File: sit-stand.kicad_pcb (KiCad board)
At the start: 2 copper layers, 158.8 x 50.8 mm, 69 parts, among them J1 USB_OTG, J2 CONN_02X03, J3 CONN_01X04, J4 CONN_01X16, J5 CONN_01X06, J6 CONN_02X04, U1 APA102, U10 APA102, U11 APA102, U12 APA102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

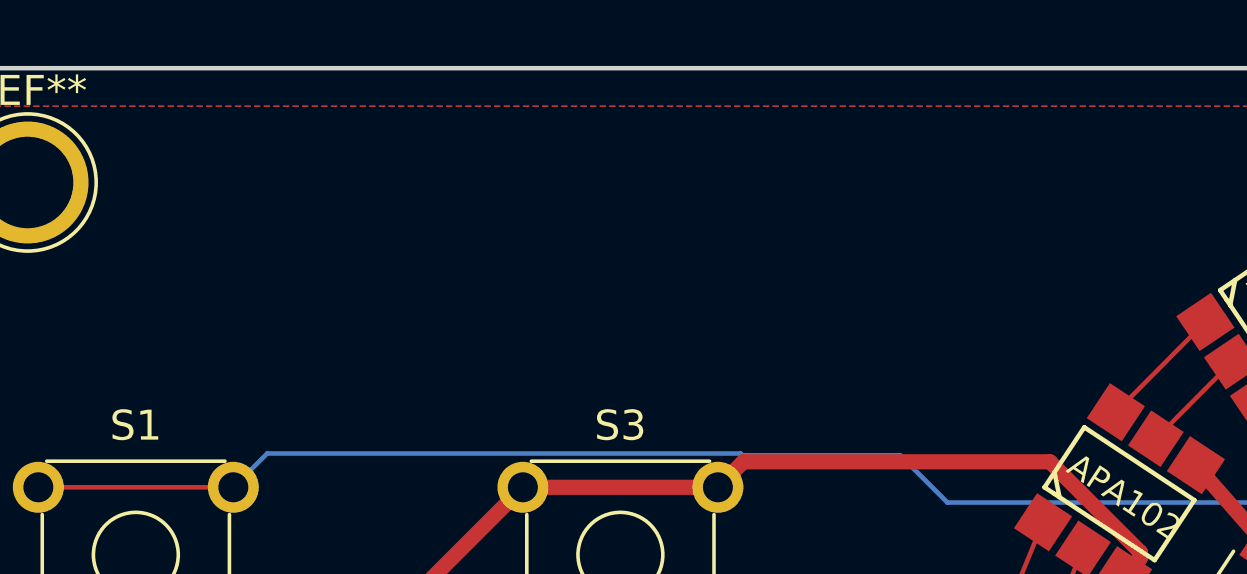
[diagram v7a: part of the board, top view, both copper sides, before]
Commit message: add text labels
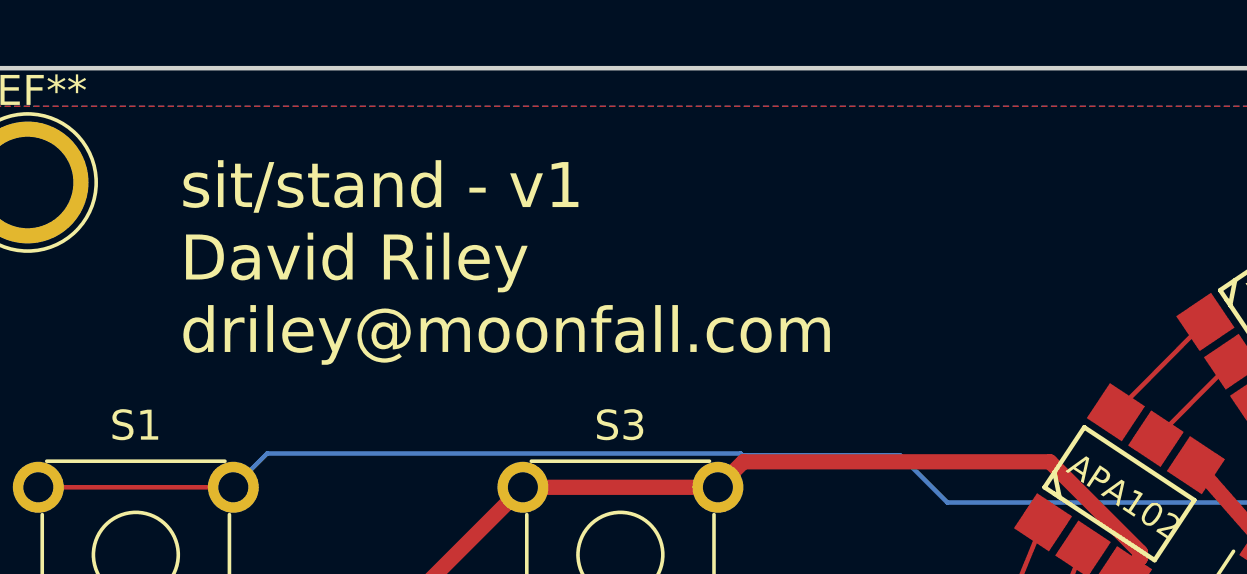
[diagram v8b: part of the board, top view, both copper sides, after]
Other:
- board text added: "sit/stand - v1 David Riley driley@moonfall.com"
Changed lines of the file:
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@@
     (area 69.749999 36.801666 231.805001 89.1825)
     (thickness 1.6002)
-    (drawings 16)
+    (drawings 18)
     (tracks 879)
     (zones 0)
@@
     (pad_to_mask_clearance 0.2)
     (aux_axis_origin 0 0)
-    (visible_elements FFFEFF7F)
+    (visible_elements FFFEFFFF)
     (pcbplotparams
       (layerselection 0x00030_80000001)
@@
     )
   )
+  (gr_text "sit/stand - v1\nDavid Riley\ndriley@moonfall.com" (at 86.36 85.09) (layer B.SilkS)
+    (effects (font (size 0.5 0.5) (thickness 0.125)) (justify left mirror))
+  )
+  (gr_text "sit/stand - v1\nDavid Riley\ndriley@moonfall.com" (at 78.74 44.45) (layer F.SilkS)
+    (effects (font (size 1.5 1.5) (thickness 0.3)) (justify left))
+  )
   (gr_line (start 228.6 86.36) (end 228.6 86.36) (layer Edge.Cuts) (width 0.15))
